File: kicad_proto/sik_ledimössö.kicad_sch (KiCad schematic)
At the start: 76 parts, among them J1 Conn_01x06_Pin, J2 Conn_01x02_Pin, U1 ATtiny861A-S

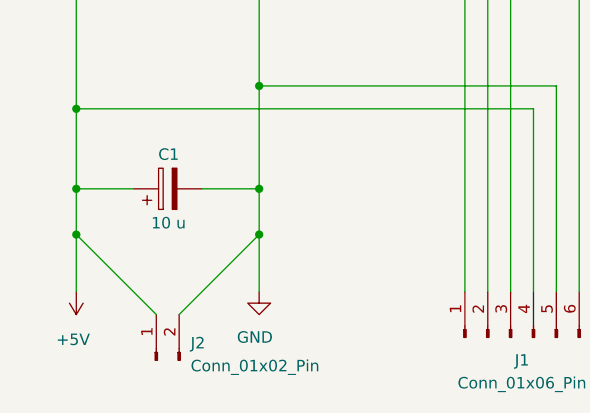
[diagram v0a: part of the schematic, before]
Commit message: Edistystä*
Paremman leiskan teko aloitettu.

Alustavat koodit valmiina.
Osa kopsattu ja muokattu Elektroniikkakerhon LED-merkki reposta.

Protolevy kokoonpanossa.
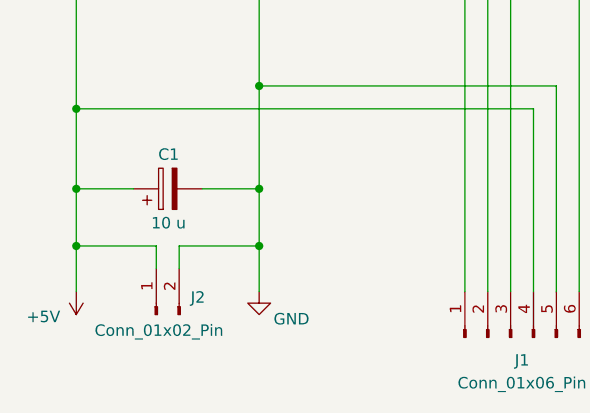
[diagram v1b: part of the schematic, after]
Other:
- moved on the sheet: J2
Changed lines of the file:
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@@
 	)
 	(junction
-		(at 34.29 134.62)
-		(diameter 0)
-		(color 0 0 0 0)
-	)
-	(junction
 		(at 207.01 77.47)
 		(diameter 0)
@@
 	)
 	(junction
+		(at 34.29 135.89)
+		(diameter 0)
+		(color 0 0 0 0)
+	)
+	(junction
 		(at 214.63 46.99)
 		(diameter 0)
@@
 	)
 	(junction
-		(at 54.61 134.62)
-		(diameter 0)
-		(color 0 0 0 0)
-	)
-	(junction
 		(at 54.61 29.21)
 		(diameter 0)
@@
 	)
 	(junction
+		(at 54.61 135.89)
+		(diameter 0)
+		(color 0 0 0 0)
+	)
+	(junction
 		(at 226.06 39.37)
 		(diameter 0)
@@
 	(wire
 		(pts
-			(xy 34.29 134.62) (xy 34.29 140.97)
-		)
-		(stroke
-			(width 0)
-			(type default)
-		)
-	)
-	(wire
-		(pts
 			(xy 207.01 110.49) (xy 207.01 115.57)
 		)
@@
 	(wire
 		(pts
-			(xy 45.72 143.51) (xy 54.61 134.62)
-		)
-		(stroke
-			(width 0)
-			(type default)
-		)
-	)
-	(wire
-		(pts
 			(xy 157.48 97.79) (xy 160.02 97.79)
 		)
@@
 	(wire
 		(pts
+			(xy 34.29 135.89) (xy 34.29 140.97)
+		)
+		(stroke
+			(width 0)
+			(type default)
+		)
+	)
+	(wire
+		(pts
 			(xy 271.78 110.49) (xy 271.78 123.19)
 		)
@@
 	(wire
 		(pts
-			(xy 54.61 129.54) (xy 54.61 134.62)
-		)
-		(stroke
-			(width 0)
-			(type default)
-		)
-	)
-	(wire
-		(pts
 			(xy 72.39 49.53) (xy 133.35 49.53)
 		)
@@
 	(wire
 		(pts
+			(xy 34.29 135.89) (xy 43.18 135.89)
+		)
+		(stroke
+			(width 0)
+			(type default)
+		)
+	)
+	(wire
+		(pts
 			(xy 205.74 34.29) (xy 207.01 34.29)
 		)
@@
 	(wire
 		(pts
+			(xy 54.61 129.54) (xy 54.61 135.89)
+		)
+		(stroke
+			(width 0)
+			(type default)
+		)
+	)
+	(wire
+		(pts
 			(xy 157.48 72.39) (xy 157.48 59.69)
 		)
@@
 	(wire
 		(pts
-			(xy 43.18 143.51) (xy 34.29 134.62)
-		)
-		(stroke
-			(width 0)
-			(type default)
-		)
-	)
-	(wire
-		(pts
 			(xy 214.63 46.99) (xy 214.63 59.69)
 		)
@@
 	(wire
 		(pts
-			(xy 54.61 134.62) (xy 54.61 140.97)
-		)
-		(stroke
-			(width 0)
-			(type default)
-		)
-	)
-	(wire
-		(pts
 			(xy 214.63 59.69) (xy 217.17 59.69)
 		)
@@
 	(wire
 		(pts
+			(xy 43.18 135.89) (xy 43.18 138.43)
+		)
+		(stroke
+			(width 0)
+			(type default)
+		)
+	)
+	(wire
+		(pts
 			(xy 243.84 46.99) (xy 245.11 46.99)
 		)
@@
 	(wire
 		(pts
+			(xy 54.61 135.89) (xy 54.61 140.97)
+		)
+		(stroke
+			(width 0)
+			(type default)
+		)
+	)
+	(wire
+		(pts
 			(xy 195.58 123.19) (xy 198.12 123.19)
 		)
@@
 	(wire
 		(pts
+			(xy 45.72 135.89) (xy 45.72 138.43)
+		)
+		(stroke
+			(width 0)
+			(type default)
+		)
+	)
+	(wire
+		(pts
 			(xy 252.73 146.05) (xy 252.73 123.19)
 		)
@@
 	(wire
 		(pts
+			(xy 45.72 135.89) (xy 54.61 135.89)
+		)
+		(stroke
+			(width 0)
+			(type default)
+		)
+	)
+	(wire
+		(pts
 			(xy 264.16 85.09) (xy 264.16 90.17)
 		)
@@
 	(wire
 		(pts
-			(xy 34.29 129.54) (xy 34.29 134.62)
+			(xy 34.29 129.54) (xy 34.29 135.89)
 		)
 		(stroke
@@
 		)
 		(property "Value" "+5V"
-			(at 35.814 146.304 0)
+			(at 32.512 143.764 0)
 			(effects
 				(font
@@
 	(symbol
 		(lib_id "Connector:Conn_01x02_Pin")
-		(at 43.18 148.59 90)
+		(at 43.18 143.51 90)
 		(unit 1)
 		(exclude_from_sim no)
@@
 		(on_board yes)
 		(dnp no)
-		(fields_autoplaced yes)
 		(property "Reference" "J2"
-			(at 46.99 146.6849 90)
+			(at 46.99 141.6049 90)
 			(effects
 				(font
@@
 		)
 		(property "Value" "Conn_01x02_Pin"
-			(at 46.99 149.2249 90)
+			(at 36.322 145.288 90)
 			(effects
 				(font
@@
 		)
 		(property "Footprint" "Connector_PinHeader_2.00mm:PinHeader_1x02_P2.00mm_Vertical"
-			(at 43.18 148.59 0)
+			(at 43.18 143.51 0)
 			(effects
 				(font
@@
 		)
 		(property "Datasheet" "~"
-			(at 43.18 148.59 0)
+			(at 43.18 143.51 0)
 			(effects
 				(font
@@
 		)
 		(property "Description" "Generic connector, single row, 01x02, script generated"
-			(at 43.18 148.59 0)
+			(at 43.18 143.51 0)
 			(effects
 				(font
@@
 		)
 		(property "Value" "GND"
-			(at 56.134 146.05 0)
+			(at 60.198 144.018 0)
 			(effects
 				(font
